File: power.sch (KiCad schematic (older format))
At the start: 29 parts, among them U1 68000D, U10 74LS244, U11 74LS373, U12 74LS244, U13 74LS373, U2 FAT_AGNUS_8375, U32 74LS139, U34 74LS373, U35 74LS244, U36 74LS05, U37 74LS32, U5 GARY_5719, X1 XTAL

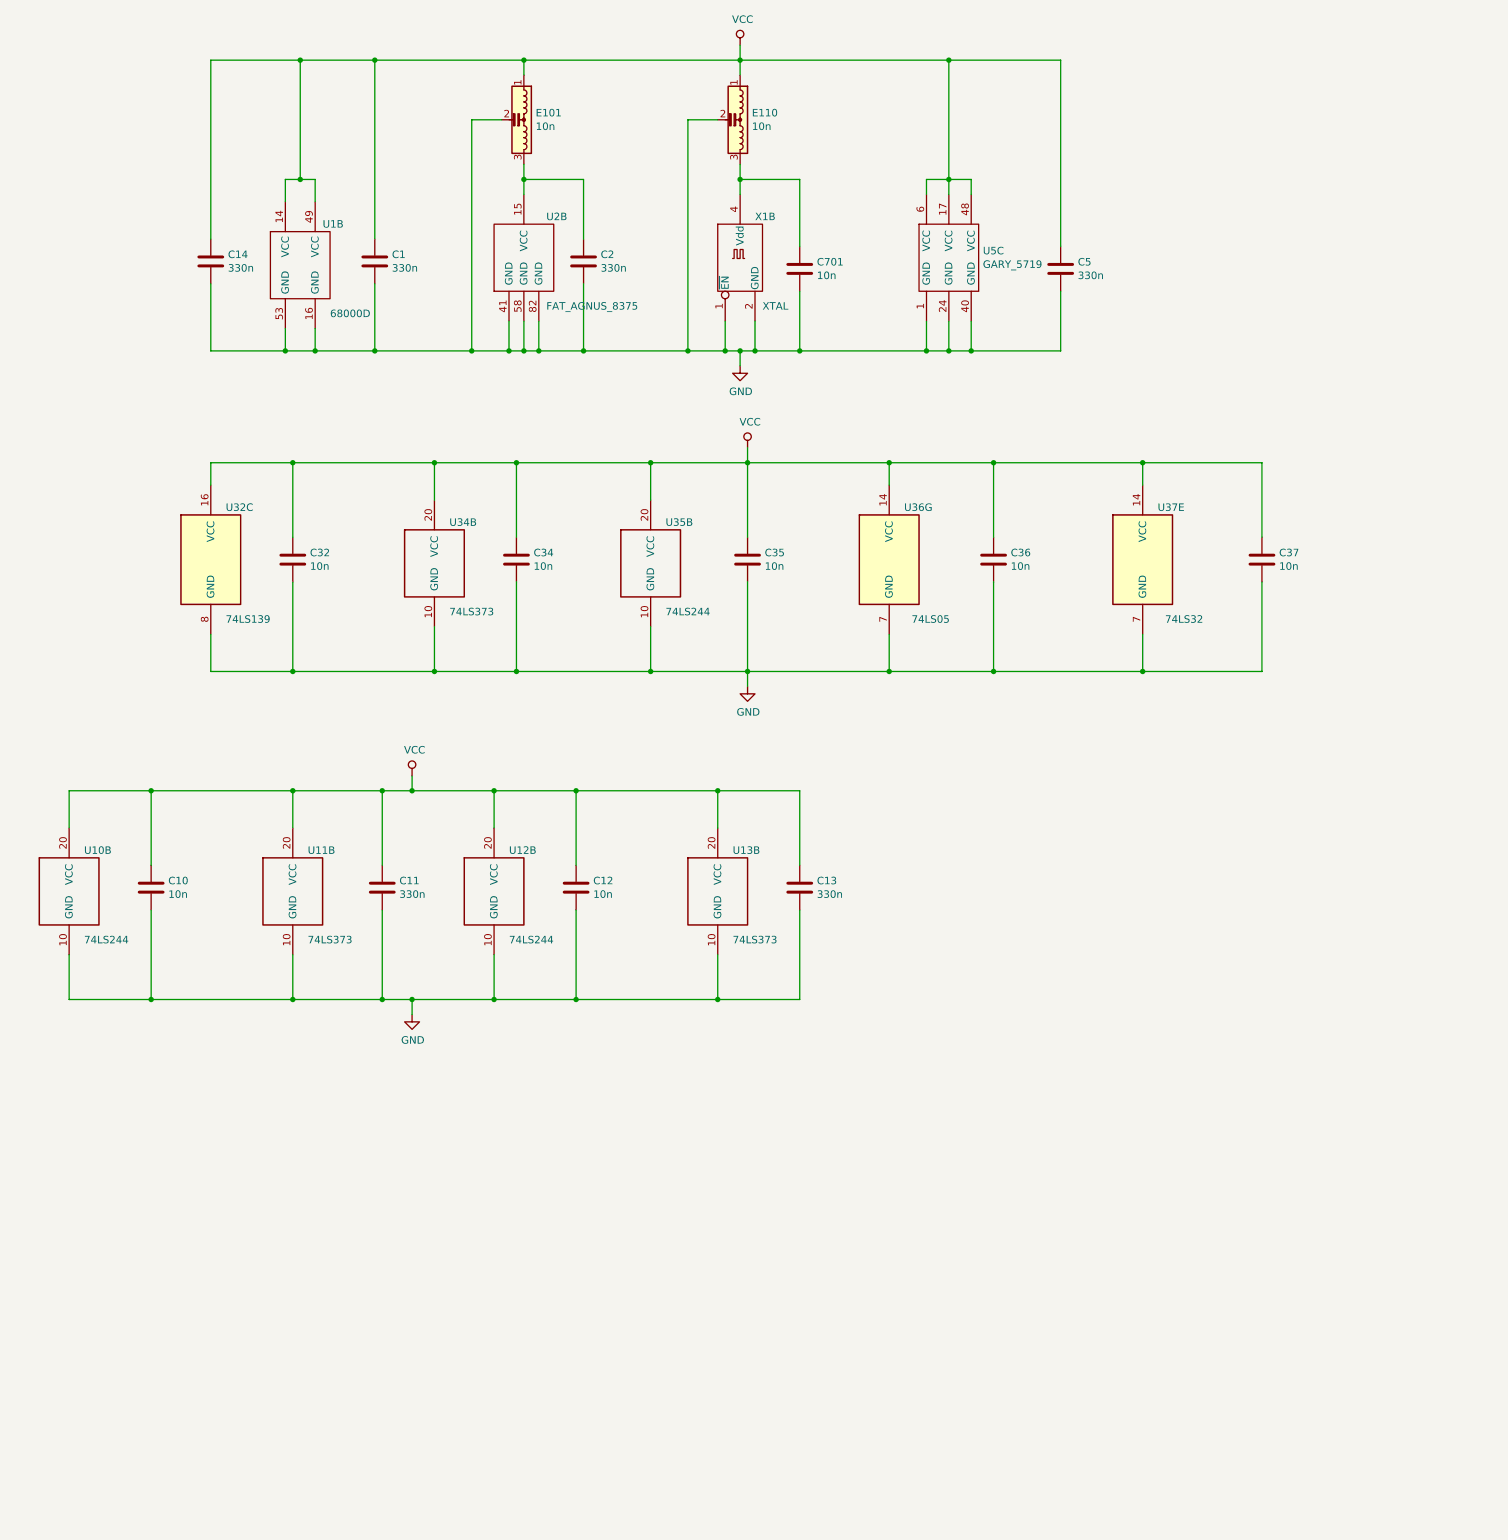
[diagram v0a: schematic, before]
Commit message: Add power input and complete clock distribution
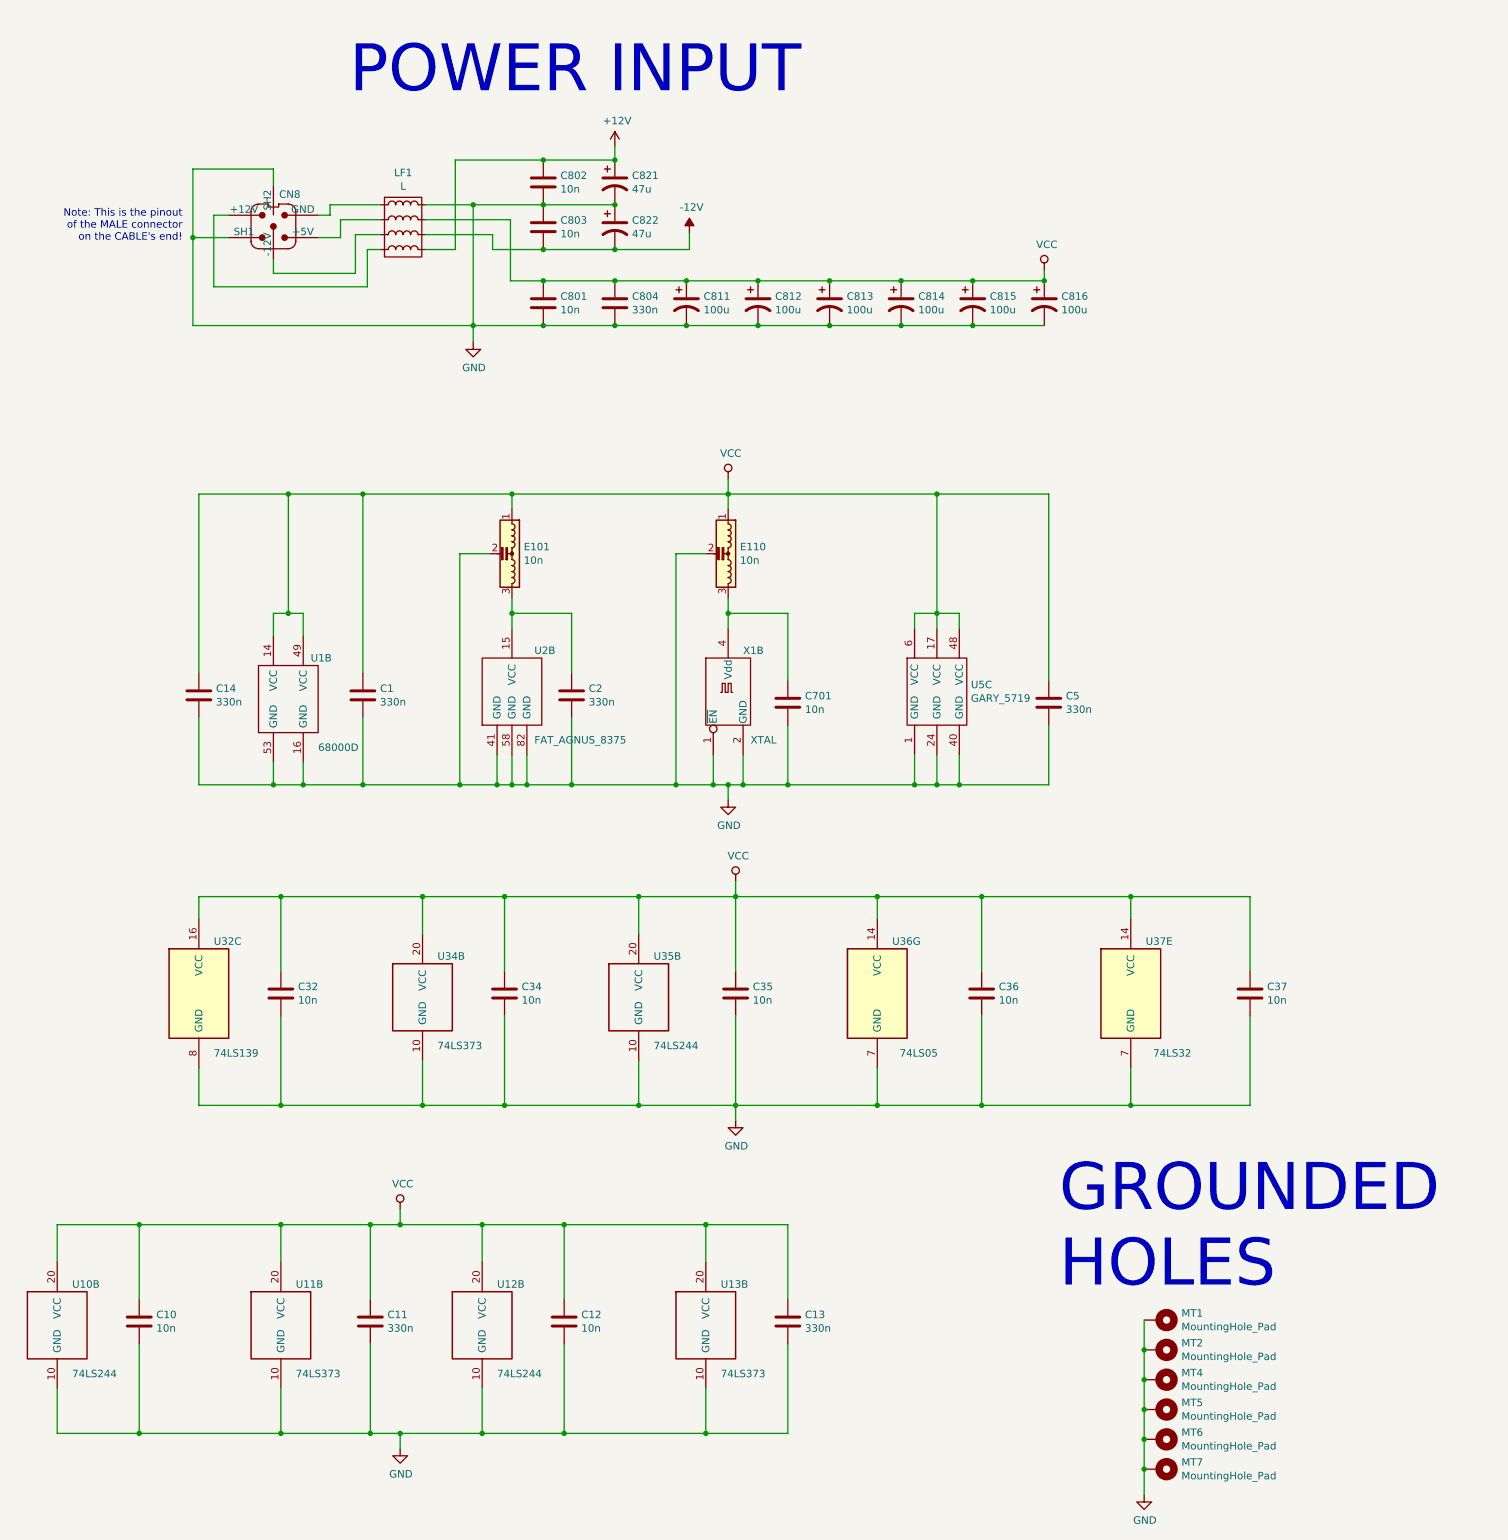
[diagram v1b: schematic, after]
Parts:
- added C801, C802, C803: 10n, symbol Device:C
- added C804: 330n, symbol Device:C
- added C811, C812, C813, C814, C815, C816: 100u, symbol Device:CP1
- added C821, C822: 47u, symbol Device:CP1
- added CN8: Power_Conn, symbol amipower:Amiga_Power_Conn
- added LF1: L, symbol linefilter:L
- added MT1, MT2, MT4, MT5, MT6, MT7: MountingHole_Pad, symbol Mechanical:MountingHole_Pad
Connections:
- net GND: now also C801.2, C802.2, C803.1, C804.2, C811.2, C812.2, C813.2, C814.2, C815.2, C816.2, C821.2, C822.1, CN8.2 (SH1), CN8.6 (SH2), LF1.8, MT1.1, MT2.1, MT4.1, MT5.1, MT6.1, MT7.1
- net VCC: now also C801.1, C804.1, C811.1, C812.1, C813.1, C814.1, C815.1, C816.1, LF1.7
- new net: CN8.1 (+5V), LF1.2
- new net: CN8.3 (+12V), LF1.4
- new net: CN8.4 (GND), LF1.1
- new net: CN8.5 (-12V), LF1.3
- new net +12V: C802.1, C821.1, LF1.5
- new net -12V: C803.2, C822.2, LF1.6
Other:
- note added: "GROUNDED\nHOLES"
- note added: "Note: This is the pinout\nof the MALE connector\non the CABLE's end!"
- note added: "POWER INPUT"
- moved on the sheet: C1, C10, C11, C12, C13, C14, C2, C32, C34, C35, C36, C37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

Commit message: Add RTC
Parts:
- C811, C812, C813, C814, C815, C816, C821, C822: footprint (none) -> Capacitor_THT:CP_Radial_D8.0mm_P5.00mm
- MT1, MT2, MT4, MT5, MT6, MT7: footprint (none) -> MountingHole:MountingHole_4mm_Pad
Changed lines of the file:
@@
 $Descr A3 16535 11693
 encoding utf-8
-Sheet 12 12
+Sheet 12 13
 Title "Rämixx500"
 Date "2019-04-20"
@@
 F 0 "C821" H 5225 1666 50  0000 L CNN
 F 1 "47u" H 5225 1575 50  0000 L CNN
-F 2 "" H 5110 1620 50  0001 C CNN
+F 2 "Capacitor_THT:CP_Radial_D8.0mm_P5.00mm" H 5110 1620 50  0001 C CNN
 F 3 "~" H 5110 1620 50  0001 C CNN
 	1    5110 1620
@@
 F 0 "C822" H 5225 1966 50  0000 L CNN
 F 1 "47u" H 5225 1875 50  0000 L CNN
-F 2 "" H 5110 1920 50  0001 C CNN
+F 2 "Capacitor_THT:CP_Radial_D8.0mm_P5.00mm" H 5110 1920 50  0001 C CNN
 F 3 "~" H 5110 1920 50  0001 C CNN
 	1    5110 1920
@@
 P 5110 1380
 AR Path="/5D2DC3A1/5CD1463C" Ref="#PWR?"  Part="1"
-AR Path="/5E9E4C57/5CD1463C" Ref="#PWR?"  Part="1"
-F 0 "#PWR?" H 5110 1230 50  0001 C CNN
+AR Path="/5E9E4C57/5CD1463C" Ref="#PWR0241"  Part="1"
+F 0 "#PWR0241" H 5110 1230 50  0001 C CNN
 F 1 "+12V" H 5125 1553 50  0000 C CNN
 F 2 "" H 5110 1380 50  0001 C CNN
@@
 P 5610 1960
 AR Path="/5D2DC3A1/5CD1464C" Ref="#PWR?"  Part="1"
-AR Path="/5E9E4C57/5CD1464C" Ref="#PWR?"  Part="1"
-F 0 "#PWR?" H 5610 2060 50  0001 C CNN
+AR Path="/5E9E4C57/5CD1464C" Ref="#PWR0242"  Part="1"
+F 0 "#PWR0242" H 5610 2060 50  0001 C CNN
 F 1 "-12V" H 5625 2133 50  0000 C CNN
 F 2 "" H 5610 1960 50  0001 C CNN
@@
 	4160 2580 4160 2690
 $Comp
-L power:GND #PWR?
+L power:GND #PWR0243
 U 1 1 5CD71648
 P 4160 2690
-F 0 "#PWR?" H 4160 2440 50  0001 C CNN
+F 0 "#PWR0243" H 4160 2440 50  0001 C CNN
 F 1 "GND" H 4165 2517 50  0000 C CNN
 F 2 "" H 4160 2690 50  0001 C CNN
@@
 F 0 "C811" H 5705 2476 50  0000 L CNN
 F 1 "100u" H 5705 2385 50  0000 L CNN
-F 2 "" H 5590 2430 50  0001 C CNN
+F 2 "Capacitor_THT:CP_Radial_D8.0mm_P5.00mm" H 5590 2430 50  0001 C CNN
 F 3 "~" H 5590 2430 50  0001 C CNN
 	1    5590 2430
@@
 F 0 "C812" H 6185 2476 50  0000 L CNN
 F 1 "100u" H 6185 2385 50  0000 L CNN
-F 2 "" H 6070 2430 50  0001 C CNN
+F 2 "Capacitor_THT:CP_Radial_D8.0mm_P5.00mm" H 6070 2430 50  0001 C CNN
 F 3 "~" H 6070 2430 50  0001 C CNN
 	1    6070 2430
@@
 F 0 "C813" H 6665 2476 50  0000 L CNN
 F 1 "100u" H 6665 2385 50  0000 L CNN
-F 2 "" H 6550 2430 50  0001 C CNN
+F 2 "Capacitor_THT:CP_Radial_D8.0mm_P5.00mm" H 6550 2430 50  0001 C CNN
 F 3 "~" H 6550 2430 50  0001 C CNN
 	1    6550 2430
@@
 F 0 "C814" H 7145 2476 50  0000 L CNN
 F 1 "100u" H 7145 2385 50  0000 L CNN
-F 2 "" H 7030 2430 50  0001 C CNN
+F 2 "Capacitor_THT:CP_Radial_D8.0mm_P5.00mm" H 7030 2430 50  0001 C CNN
 F 3 "~" H 7030 2430 50  0001 C CNN
 	1    7030 2430
@@
 F 0 "C815" H 7625 2476 50  0000 L CNN
 F 1 "100u" H 7625 2385 50  0000 L CNN
-F 2 "" H 7510 2430 50  0001 C CNN
+F 2 "Capacitor_THT:CP_Radial_D8.0mm_P5.00mm" H 7510 2430 50  0001 C CNN
 F 3 "~" H 7510 2430 50  0001 C CNN
 	1    7510 2430
@@
 F 0 "C816" H 8105 2476 50  0000 L CNN
 F 1 "100u" H 8105 2385 50  0000 L CNN
-F 2 "" H 7990 2430 50  0001 C CNN
+F 2 "Capacitor_THT:CP_Radial_D8.0mm_P5.00mm" H 7990 2430 50  0001 C CNN
 F 3 "~" H 7990 2430 50  0001 C CNN
 	1    7990 2430
@@
 	7510 2280 7990 2280
 $Comp
-L power:VCC #PWR?
+L power:VCC #PWR0244
 U 1 1 5CDB4D2E
 P 7990 2210
-F 0 "#PWR?" H 7990 2060 50  0001 C CNN
+F 0 "#PWR0244" H 7990 2060 50  0001 C CNN
 F 1 "VCC" H 8007 2383 50  0000 C CNN
 F 2 "" H 7990 2210 50  0001 C CNN
@@
 F 0 "MT1" V 8714 9400 50  0000 L CNN
 F 1 "MountingHole_Pad" V 8805 9400 50  0000 L CNN
-F 2 "" H 8760 9250 50  0001 C CNN
+F 2 "MountingHole:MountingHole_4mm_Pad" H 8760 9250 50  0001 C CNN
 F 3 "~" H 8760 9250 50  0001 C CNN
 	1    8760 9250
@@
 F 0 "MT2" V 8714 9600 50  0000 L CNN
 F 1 "MountingHole_Pad" V 8805 9600 50  0000 L CNN
-F 2 "" H 8760 9450 50  0001 C CNN
+F 2 "MountingHole:MountingHole_4mm_Pad" H 8760 9450 50  0001 C CNN
 F 3 "~" H 8760 9450 50  0001 C CNN
 	1    8760 9450
@@
 F 0 "MT4" V 8714 9800 50  0000 L CNN
 F 1 "MountingHole_Pad" V 8805 9800 50  0000 L CNN
-F 2 "" H 8760 9650 50  0001 C CNN
+F 2 "MountingHole:MountingHole_4mm_Pad" H 8760 9650 50  0001 C CNN
 F 3 "~" H 8760 9650 50  0001 C CNN
 	1    8760 9650
@@
 F 0 "MT5" V 8714 10000 50  0000 L CNN
 F 1 "MountingHole_Pad" V 8805 10000 50  0000 L CNN
-F 2 "" H 8760 9850 50  0001 C CNN
+F 2 "MountingHole:MountingHole_4mm_Pad" H 8760 9850 50  0001 C CNN
 F 3 "~" H 8760 9850 50  0001 C CNN
 	1    8760 9850
@@
 F 0 "MT6" V 8714 10200 50  0000 L CNN
 F 1 "MountingHole_Pad" V 8805 10200 50  0000 L CNN
-F 2 "" H 8760 10050 50  0001 C CNN
+F 2 "MountingHole:MountingHole_4mm_Pad" H 8760 10050 50  0001 C CNN
 F 3 "~" H 8760 10050 50  0001 C CNN
 	1    8760 10050
@@
 F 0 "MT7" V 8714 10400 50  0000 L CNN
 F 1 "MountingHole_Pad" V 8805 10400 50  0000 L CNN
-F 2 "" H 8760 10250 50  0001 C CNN
+F 2 "MountingHole:MountingHole_4mm_Pad" H 8760 10250 50  0001 C CNN
 F 3 "~" H 8760 10250 50  0001 C CNN
 	1    8760 10250
@@
 	8660 10250 8660 10420
 $Comp
-L power:GND #PWR?
+L power:GND #PWR0245
 U 1 1 5CE0CCBE
 P 8660 10420
-F 0 "#PWR?" H 8660 10170 50  0001 C CNN
+F 0 "#PWR0245" H 8660 10170 50  0001 C CNN
 F 1 "GND" H 8665 10247 50  0000 C CNN
 F 2 "" H 8660 10420 50  0001 C CNN

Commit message: Fix power-up reset
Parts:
- C1, C10, C11, C12, C13, C14, C2, C32, C34, C35, C36, C37, C5: footprint (none) -> Raemixx500:C_Axial_L6.3mm_D2.5mm_P10.16mm
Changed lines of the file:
@@
 EESchema Schematic File Version 4
 LIBS:Raemix500-cache
-EELAYER 26 0
+EELAYER 29 0
 EELAYER END
 $Descr A3 16535 11693
@@
 F 0 "C14" H 2435 5106 50  0000 L CNN
 F 1 "330n" H 2435 5015 50  0000 L CNN
-F 2 "" H 2358 4910 50  0001 C CNN
+F 2 "Raemixx500:C_Axial_L6.3mm_D2.5mm_P10.16mm" H 2358 4910 50  0001 C CNN
 F 3 "~" H 2320 5060 50  0001 C CNN
 	1    2320 5060
@@
 F 0 "C1" H 3535 5106 50  0000 L CNN
 F 1 "330n" H 3535 5015 50  0000 L CNN
-F 2 "" H 3458 4910 50  0001 C CNN
+F 2 "Raemixx500:C_Axial_L6.3mm_D2.5mm_P10.16mm" H 3458 4910 50  0001 C CNN
 F 3 "~" H 3420 5060 50  0001 C CNN
 	1    3420 5060
@@
 F 0 "C2" H 4935 5106 50  0000 L CNN
 F 1 "330n" H 4935 5015 50  0000 L CNN
-F 2 "" H 4858 4910 50  0001 C CNN
+F 2 "Raemixx500:C_Axial_L6.3mm_D2.5mm_P10.16mm" H 4858 4910 50  0001 C CNN
 F 3 "~" H 4820 5060 50  0001 C CNN
 	1    4820 5060
@@
 F 0 "C5" H 8135 5156 50  0000 L CNN
 F 1 "330n" H 8135 5065 50  0000 L CNN
-F 2 "" H 8058 4960 50  0001 C CNN
+F 2 "Raemixx500:C_Axial_L6.3mm_D2.5mm_P10.16mm" H 8058 4960 50  0001 C CNN
 F 3 "~" H 8020 5110 50  0001 C CNN
 	1    8020 5110
@@
 F 0 "C11" H 3585 9306 50  0000 L CNN
 F 1 "330n" H 3585 9215 50  0000 L CNN
-F 2 "" H 3508 9110 50  0001 C CNN
+F 2 "Raemixx500:C_Axial_L6.3mm_D2.5mm_P10.16mm" H 3508 9110 50  0001 C CNN
 F 3 "~" H 3470 9260 50  0001 C CNN
 	1    3470 9260
@@
 F 0 "C13" H 6385 9306 50  0000 L CNN
 F 1 "330n" H 6385 9215 50  0000 L CNN
-F 2 "" H 6308 9110 50  0001 C CNN
+F 2 "Raemixx500:C_Axial_L6.3mm_D2.5mm_P10.16mm" H 6308 9110 50  0001 C CNN
 F 3 "~" H 6270 9260 50  0001 C CNN
 	1    6270 9260
@@
 F 0 "C10" H 2035 9306 50  0000 L CNN
 F 1 "10n" H 2035 9215 50  0000 L CNN
-F 2 "" H 1958 9110 50  0001 C CNN
+F 2 "Raemixx500:C_Axial_L6.3mm_D2.5mm_P10.16mm" H 1958 9110 50  0001 C CNN
 F 3 "~" H 1920 9260 50  0001 C CNN
 	1    1920 9260
@@
 F 0 "C12" H 4885 9306 50  0000 L CNN
 F 1 "10n" H 4885 9215 50  0000 L CNN
-F 2 "" H 4808 9110 50  0001 C CNN
+F 2 "Raemixx500:C_Axial_L6.3mm_D2.5mm_P10.16mm" H 4808 9110 50  0001 C CNN
 F 3 "~" H 4770 9260 50  0001 C CNN
 	1    4770 9260
@@
 F 0 "C32" H 2985 7106 50  0000 L CNN
 F 1 "10n" H 2985 7015 50  0000 L CNN
-F 2 "" H 2908 6910 50  0001 C CNN
+F 2 "Raemixx500:C_Axial_L6.3mm_D2.5mm_P10.16mm" H 2908 6910 50  0001 C CNN
 F 3 "~" H 2870 7060 50  0001 C CNN
 	1    2870 7060
@@
 F 0 "C34" H 4485 7106 50  0000 L CNN
 F 1 "10n" H 4485 7015 50  0000 L CNN
-F 2 "" H 4408 6910 50  0001 C CNN
+F 2 "Raemixx500:C_Axial_L6.3mm_D2.5mm_P10.16mm" H 4408 6910 50  0001 C CNN
 F 3 "~" H 4370 7060 50  0001 C CNN
 	1    4370 7060
@@
 F 0 "C35" H 6035 7106 50  0000 L CNN
 F 1 "10n" H 6035 7015 50  0000 L CNN
-F 2 "" H 5958 6910 50  0001 C CNN
+F 2 "Raemixx500:C_Axial_L6.3mm_D2.5mm_P10.16mm" H 5958 6910 50  0001 C CNN
 F 3 "~" H 5920 7060 50  0001 C CNN
 	1    5920 7060
@@
 F 0 "C36" H 7685 7106 50  0000 L CNN
 F 1 "10n" H 7685 7015 50  0000 L CNN
-F 2 "" H 7608 6910 50  0001 C CNN
+F 2 "Raemixx500:C_Axial_L6.3mm_D2.5mm_P10.16mm" H 7608 6910 50  0001 C CNN
 F 3 "~" H 7570 7060 50  0001 C CNN
 	1    7570 7060
@@
 F 0 "C37" H 9485 7106 50  0000 L CNN
 F 1 "10n" H 9485 7015 50  0000 L CNN
-F 2 "" H 9408 6910 50  0001 C CNN
+F 2 "Raemixx500:C_Axial_L6.3mm_D2.5mm_P10.16mm" H 9408 6910 50  0001 C CNN
 F 3 "~" H 9370 7060 50  0001 C CNN
 	1    9370 7060

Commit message: Work in progress
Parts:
- CN8: footprint (none) -> w_conn_av:din-5
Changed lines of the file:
@@
 F 0 "CN8" H 2930 2180 50  0000 C CNN
 F 1 "Power_Conn" H 2680 2280 50  0001 C CNN
-F 2 "" H 870 2390 50  0001 C CNN
+F 2 "w_conn_av:din-5" H 870 2390 50  0001 C CNN
 F 3 "~" H 870 2390 50  0001 C CNN
 	1    2820 1940

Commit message: Work in progress
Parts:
- C801, C802, C803, C804: footprint (none) -> Raemixx500:C_Axial_L6.3mm_D2.5mm_P10.16mm
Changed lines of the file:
@@
 F 0 "C802" H 4745 1666 50  0000 L CNN
 F 1 "10n" H 4745 1575 50  0000 L CNN
-F 2 "" H 4668 1470 50  0001 C CNN
+F 2 "Raemixx500:C_Axial_L6.3mm_D2.5mm_P10.16mm" H 4668 1470 50  0001 C CNN
 F 3 "~" H 4630 1620 50  0001 C CNN
 	1    4630 1620
@@
 F 0 "C803" H 4745 1966 50  0000 L CNN
 F 1 "10n" H 4745 1875 50  0000 L CNN
-F 2 "" H 4668 1770 50  0001 C CNN
+F 2 "Raemixx500:C_Axial_L6.3mm_D2.5mm_P10.16mm" H 4668 1770 50  0001 C CNN
 F 3 "~" H 4630 1920 50  0001 C CNN
 	1    4630 1920
@@
 F 0 "C801" H 4745 2476 50  0000 L CNN
 F 1 "10n" H 4745 2385 50  0000 L CNN
-F 2 "" H 4668 2280 50  0001 C CNN
+F 2 "Raemixx500:C_Axial_L6.3mm_D2.5mm_P10.16mm" H 4668 2280 50  0001 C CNN
 F 3 "~" H 4630 2430 50  0001 C CNN
 	1    4630 2430
@@
 F 0 "C804" H 5225 2476 50  0000 L CNN
 F 1 "330n" H 5225 2385 50  0000 L CNN
-F 2 "" H 5148 2280 50  0001 C CNN
+F 2 "Raemixx500:C_Axial_L6.3mm_D2.5mm_P10.16mm" H 5148 2280 50  0001 C CNN
 F 3 "~" H 5110 2430 50  0001 C CNN
 	1    5110 2430
